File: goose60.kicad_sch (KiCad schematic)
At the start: 29 parts, among them SW1 SW_Push, SW2 SW_Push, U1 STM32F103CBTx, X1 Crystal_GND24

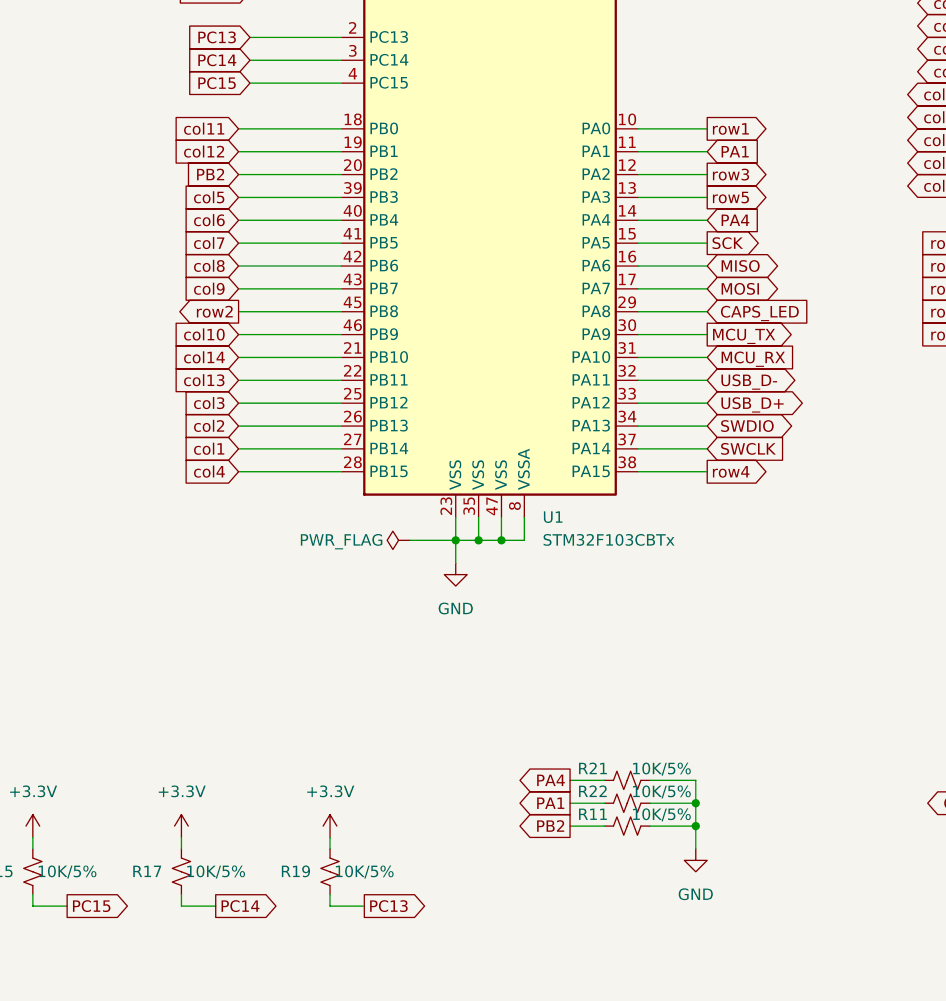
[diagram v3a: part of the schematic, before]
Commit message: change MCU location and change row5 pin
* row5 -> PB2
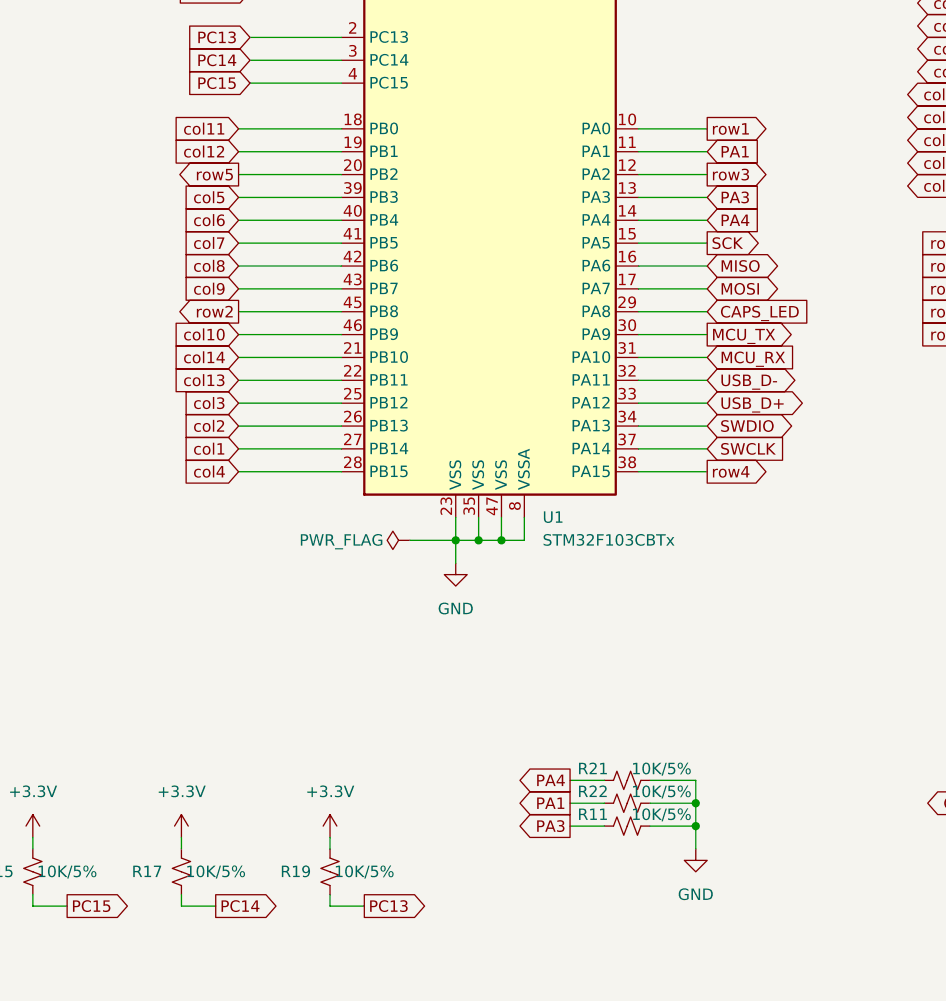
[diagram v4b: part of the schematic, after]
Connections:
- net row5: now also U1.20 (PB2); no longer U1.13 (PA3)
- net PB2 renamed PA3
- net PA3: now also U1.13 (PA3); no longer U1.20 (PB2)
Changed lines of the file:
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@@
     )
   )
-  (global_label "PB2" (shape output) (at 193.04 142.24 180) (fields_autoplaced)
-    (effects (font (size 1.27 1.27)) (justify right))
-    (property "插入圖紙頁參考" "${INTERSHEET_REFS}" (id 0) (at 186.8774 142.1606 0)
+  (global_label "PA3" (shape output) (at 193.04 142.24 180) (fields_autoplaced)
+    (effects (font (size 1.27 1.27)) (justify right))
+    (property "插入圖紙頁參考" "${INTERSHEET_REFS}" (id 0) (at 187.0588 142.1606 0)
       (effects (font (size 1.27 1.27)) (justify right) hide)
     )
@@
     )
   )
-  (global_label "PB2" (shape input) (at 156.21 69.85 180) (fields_autoplaced)
-    (effects (font (size 1.27 1.27)) (justify right))
-    (property "插入圖紙頁參考" "${INTERSHEET_REFS}" (id 0) (at 150.0474 69.7706 0)
-      (effects (font (size 1.27 1.27)) (justify right) hide)
-    )
-  )
   (global_label "USB_D-" (shape bidirectional) (at 208.28 92.71 0) (fields_autoplaced)
     (effects (font (size 1.27 1.27)) (justify left))
@@
     )
   )
+  (global_label "PA3" (shape input) (at 208.28 72.39 0) (fields_autoplaced)
+    (effects (font (size 1.27 1.27)) (justify left))
+    (property "插入圖紙頁參考" "${INTERSHEET_REFS}" (id 0) (at 214.2612 72.3106 0)
+      (effects (font (size 1.27 1.27)) (justify left) hide)
+    )
+  )
   (global_label "PC13" (shape input) (at 157.48 54.61 180) (fields_autoplaced)
     (effects (font (size 1.27 1.27)) (justify right))
@@
     )
   )
+  (global_label "row5" (shape output) (at 156.21 69.85 180) (fields_autoplaced)
+    (effects (font (size 1.27 1.27)) (justify right))
+    (property "插入圖紙頁參考" "${INTERSHEET_REFS}" (id 0) (at 149.3217 69.9294 0)
+      (effects (font (size 1.27 1.27)) (justify right) hide)
+    )
+  )
   (global_label "SWCLK" (shape output) (at 58.42 143.51 0) (fields_autoplaced)
     (effects (font (size 1.27 1.27)) (justify left))
@@
     )
   )
-  (global_label "row5" (shape output) (at 208.28 72.39 0) (fields_autoplaced)
-    (effects (font (size 1.27 1.27)) (justify left))
-    (property "插入圖紙頁參考" "${INTERSHEET_REFS}" (id 0) (at 215.1683 72.3106 0)
-      (effects (font (size 1.27 1.27)) (justify left) hide)
-    )
-  )
